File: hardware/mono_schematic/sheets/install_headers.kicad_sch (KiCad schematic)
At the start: 66 parts

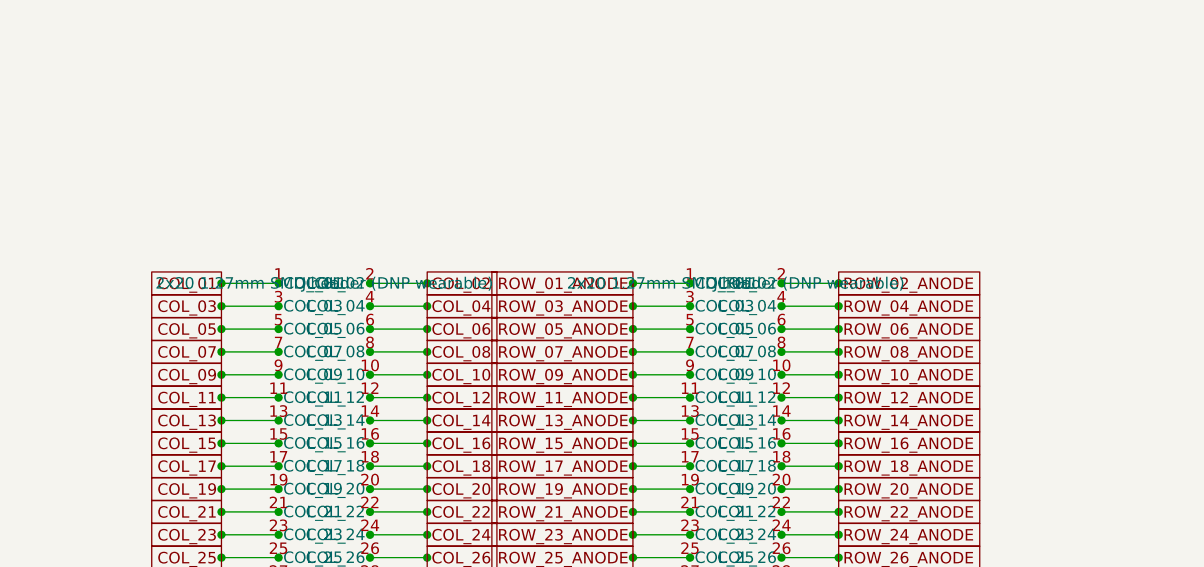
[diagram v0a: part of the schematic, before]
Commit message: mono_electronics v14b: installation headers -> XFCN BH127VS-40P-H49 2x20 1.27mm shrouded keyed box headers (C42462832; mate IDC3-40232A1EUB1 C49232620 + 0.635mm ribbon), 1:1 FFC pinout, 64 TVS kept; board 159.45x99.5 (was 160.5); gates clean; BOM/CPL variants + fab v14 regen
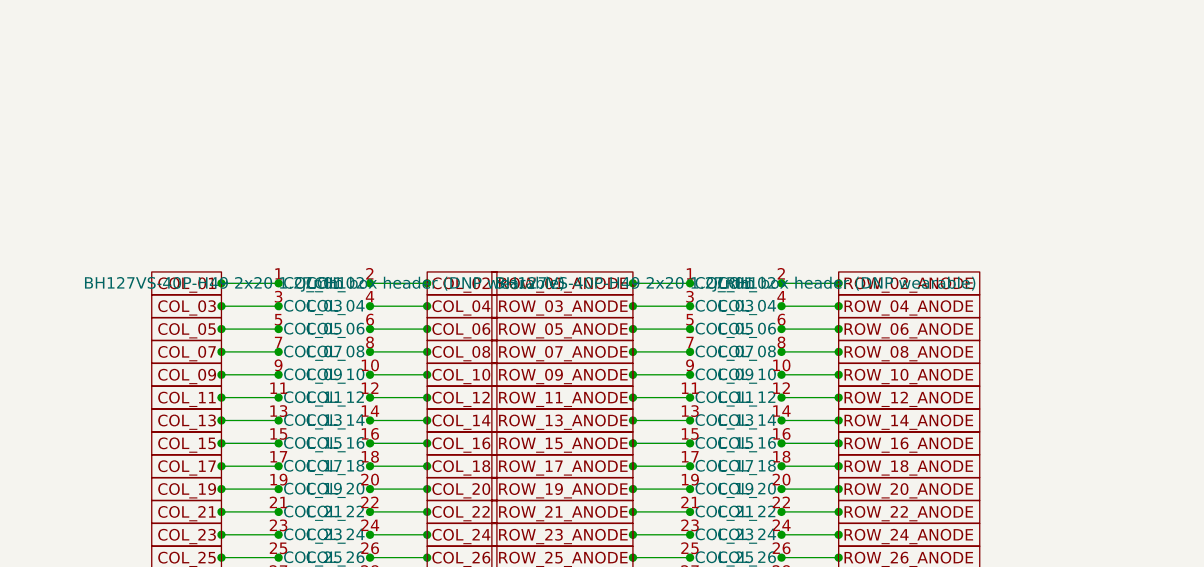
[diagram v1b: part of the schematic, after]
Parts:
- removed J_CH1, J_RH1: 2x20 1.27mm SMD header (DNP wearable), mono_electronics:PinHeader_2x20_P1.27mm_Vertical_SMD, symbol mono_parts:2x20_1.27mm_SMD_header__DNP_wearable__PinHeader_2x20_P1.27mm_Vertica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
- added J_CH1, J_RH1: BH127VS-40P-H49 2x20 1.27mm box header (DNP weara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, mono_electronics:BoxHeader_XFCN_BH127VS-40P-H49_2x20_P1.27mm_Vertical_SMD, symbol mono_parts:BH127VS-40P-H49_2x20_1.27mm_box_header__DNP_wearable__BoxHeader_XFCN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
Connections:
- net COL_01: now also J_CH1.1 (COL_01)
- net COL_02: now also J_CH1.2 (COL_02)
- net COL_03: now also J_CH1.3 (COL_03)
- net COL_04: now also J_CH1.4 (COL_04)
- net COL_05: now also J_CH1.5 (COL_05)
- net COL_06: now also J_CH1.6 (COL_06)
- net COL_07: now also J_CH1.7 (COL_07)
- net COL_08: now also J_CH1.8 (COL_08)
- net COL_09: now also J_CH1.9 (COL_09)
- net COL_10: now also J_CH1.10 (COL_10)
- net COL_11: now also J_CH1.11 (COL_11)
- net COL_12: now also J_CH1.12 (COL_12)
- net COL_13: now also J_CH1.13 (COL_13)
- net COL_14: now also J_CH1.14 (COL_14)
- net COL_15: now also J_CH1.15 (COL_15)
- net COL_16: now also J_CH1.16 (COL_16)
- net COL_17: now also J_CH1.17 (COL_17)
- net COL_18: now also J_CH1.18 (COL_18)
- net COL_19: now also J_CH1.19 (COL_19)
- net COL_20: now also J_CH1.20 (COL_20)
- net COL_21: now also J_CH1.21 (COL_21)
- net COL_22: now also J_CH1.22 (COL_22)
- net COL_23: now also J_CH1.23 (COL_23)
- net COL_24: now also J_CH1.24 (COL_24)
- net COL_25: now also J_CH1.25 (COL_25)
- net COL_26: now also J_CH1.26 (COL_26)
- net COL_27: now also J_CH1.27 (COL_27)
- net COL_28: now also J_CH1.28 (COL_28)
- net COL_29: now also J_CH1.29 (COL_29)
- net COL_30: now also J_CH1.30 (COL_30)
- net COL_31: now also J_CH1.31 (COL_31)
- net COL_32: now also J_CH1.32 (COL_32)
- net EXP_3V3: now also J_CH1.39 (EXP_3V3)
- net EXP_CLK: now also J_CH1.35 (EXP_CLK)
- net EXP_LE: now also J_CH1.36 (EXP_LE)
- net EXP_OE: now also J_CH1.37 (EXP_OE)
- net EXP_SDI: now also J_CH1.34 (EXP_SDI)
- net GND: now also J_CH1.33 (GND), J_CH1.38 (GND), J_CH1.40 (GND), J_RH1.33 (GND), J_RH1.38 (GND), J_RH1.40 (GND)
- net ID_3V3: now also J_RH1.37 (EXP_OE)
- net ID_SCL: now also J_RH1.36 (EXP_LE)
- net ID_SDA: now also J_RH1.35 (EXP_CLK)
- net ROW_01_ANODE: now also J_RH1.1 (COL_01)
- net ROW_02_ANODE: now also J_RH1.2 (COL_02)
- net ROW_03_ANODE: now also J_RH1.3 (COL_03)
- net ROW_04_ANODE: now also J_RH1.4 (COL_04)
- net ROW_05_ANODE: now also J_RH1.5 (COL_05)
- net ROW_06_ANODE: now also J_RH1.6 (COL_06)
- net ROW_07_ANODE: now also J_RH1.7 (COL_07)
- net ROW_08_ANODE: now also J_RH1.8 (COL_08)
- net ROW_09_ANODE: now also J_RH1.9 (COL_09)
- net ROW_10_ANODE: now also J_RH1.10 (COL_10)
- net ROW_11_ANODE: now also J_RH1.11 (COL_11)
- net ROW_12_ANODE: now also J_RH1.12 (COL_12)
- net ROW_13_ANODE: now also J_RH1.13 (COL_13)
- net ROW_14_ANODE: now also J_RH1.14 (COL_14)
- net ROW_15_ANODE: now also J_RH1.15 (COL_15)
- net ROW_16_ANODE: now also J_RH1.16 (COL_16)
- net ROW_17_ANODE: now also J_RH1.17 (COL_17)
- net ROW_18_ANODE: now also J_RH1.18 (COL_18)
- net ROW_19_ANODE: now also J_RH1.19 (COL_19)
- net ROW_20_ANODE: now also J_RH1.20 (COL_20)
- net ROW_21_ANODE: now also J_RH1.21 (COL_21)
- net ROW_22_ANODE: now also J_RH1.22 (COL_22)
- net ROW_23_ANODE: now also J_RH1.23 (COL_23)
- net ROW_24_ANODE: now also J_RH1.24 (COL_24)
- net ROW_25_ANODE: now also J_RH1.25 (COL_25)
- net ROW_26_ANODE: now also J_RH1.26 (COL_26)
- net ROW_27_ANODE: now also J_RH1.27 (COL_27)
- net ROW_28_ANODE: now also J_RH1.28 (COL_28)
- net ROW_29_ANODE: now also J_RH1.29 (COL_29)
- net ROW_30_ANODE: now also J_RH1.30 (COL_30)
- net ROW_31_ANODE: now also J_RH1.31 (COL_31)
- net ROW_32_ANODE: now also J_RH1.32 (COL_32)
- net ROW_SPARE_34: now also J_RH1.34 (EXP_SDI)
- net ROW_SPARE_39: now also J_RH1.39 (EXP_3V3)
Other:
- title: Installation-build cable headers (v14, DNP in wearable) - J_RH1/J_CH1 2x20 1.27 mm SMD in parallel with J_ROW1/J_COL1 pin-for-pin, PESD5V0S1BL per LED line -> Installation-build cable headers (v14, DNP in wearable) - J_RH1/J_CH1 2x20 1.27 mm shrouded keyed box headers (XFCN BH127VS-40P-H49) in parallel with J_ROW1/J_COL1 pin-for-pin, PESD5V0S1BL per LED line

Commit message: mono_electronics v15b: standalone project projects/mono_electronics_v15 (KiCad sch+pcb+libs+3D, fab, drawings, renders, docs); D_VBUS1 next to J_USB1, SYS 0.6 mm + doubled vias, 3 fiducials, silk 0.15, J_PORT courtyards inside edge, 1.6 mm JLC04161H-7628 stackup, 24 sub-0.127 mm gaps fixed (min_clearance 0.127), sch DNP/BOM attrs + lib nicknames -> native parity 0; DRC 0 ERC 0 continuity 312/312
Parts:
- D_C01, D_C02, D_C03, D_C04, D_C05, D_C06, D_C07, D_C08, D_C09, D_C10, D_C11, D_C12, D_C13, D_C14, D_C15, D_C16, D_C17, D_C18, D_C19, D_C20, D_C21, D_C22, D_C23, D_C24, D_C25, D_C26, D_C27, D_C28, D_C29, D_C30, D_C31, D_C32, D_R01, D_R02, D_R03, D_R04, D_R05, D_R06, D_R07, D_R08, D_R09, D_R10, D_R11, D_R12, D_R13, D_R14, D_R15, D_R16, D_R17, D_R18, D_R19, D_R20, D_R21, D_R22, D_R23, D_R24, D_R25, D_R26, D_R27, D_R28, D_R29, D_R30, D_R31, D_R32, J_CH1, J_RH1: now not fitted
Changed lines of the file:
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@@
     (on_board yes)
     (in_pos_files yes)
-    (dnp no)
+    (dnp yes)
     (property
       "Reference"
@@
     (on_board yes)
     (in_pos_files yes)
-    (dnp no)
+    (dnp yes)
     (property
       "Reference"
@@
     (on_board yes)
     (in_pos_files yes)
-    (dnp no)
+    (dnp yes)
     (property
       "Reference"
@@
     (on_board yes)
     (in_pos_files yes)
-    (dnp no)
+    (dnp yes)
     (property
       "Reference"
@@
     (on_board yes)
     (in_pos_files yes)
-    (dnp no)
+    (dnp yes)
     (property
       "Reference"
@@
     (on_board yes)
     (in_pos_files yes)
-    (dnp no)
+    (dnp yes)
     (property
       "Reference"
@@
     (on_board yes)
     (in_pos_files yes)
-    (dnp no)
+    (dnp yes)
     (property
       "Reference"
@@
     (on_board yes)
     (in_pos_files yes)
-    (dnp no)
+    (dnp yes)
     (property
       "Reference"
@@
     (on_board yes)
     (in_pos_files yes)
-    (dnp no)
+    (dnp yes)
     (property
       "Reference"
@@
     (on_board yes)
     (in_pos_files yes)
-    (dnp no)
+    (dnp yes)
     (property
       "Reference"
@@
     (on_board yes)
     (in_pos_files yes)
-    (dnp no)
+    (dnp yes)
     (property
       "Reference"
@@
     (on_board yes)
     (in_pos_files yes)
-    (dnp no)
+    (dnp yes)
     (property
       "Reference"
@@
     (on_board yes)
     (in_pos_files yes)
-    (dnp no)
+    (dnp yes)
     (property
       "Reference"
@@
     (on_board yes)
     (in_pos_files yes)
-    (dnp no)
+    (dnp yes)
     (property
       "Reference"
@@
     (on_board yes)
     (in_pos_files yes)
-    (dnp no)
+    (dnp yes)
     (property
       "Reference"
@@
     (on_board yes)
     (in_pos_files yes)
-    (dnp no)
+    (dnp yes)
     (property
       "Reference"
@@
     (on_board yes)
     (in_pos_files yes)
-    (dnp no)
+    (dnp yes)
     (property
       "Reference"
@@
     (on_board yes)
     (in_pos_files yes)
-    (dnp no)
+    (dnp yes)
     (property
       "Reference"
@@
     (on_board yes)
     (in_pos_files yes)
-    (dnp no)
+    (dnp yes)
     (property
       "Reference"
@@
     (on_board yes)
     (in_pos_files yes)
-    (dnp no)
+    (dnp yes)
     (property
       "Reference"
@@
     (on_board yes)
     (in_pos_files yes)
-    (dnp no)
+    (dnp yes)
     (property
       "Reference"
@@
     (on_board yes)
     (in_pos_files yes)
-    (dnp no)
+    (dnp yes)
     (property
       "Reference"
@@
     (on_board yes)
     (in_pos_files yes)
-    (dnp no)
+    (dnp yes)
     (property
       "Reference"
@@
     (on_board yes)
     (in_pos_files yes)
-    (dnp no)
+    (dnp yes)
     (property
       "Reference"
@@
     (on_board yes)
     (in_pos_files yes)
-    (dnp no)
+    (dnp yes)
     (property
       "Reference"
@@
     (on_board yes)
     (in_pos_files yes)
-    (dnp no)
+    (dnp yes)
     (property
       "Reference"
@@
     (on_board yes)
     (in_pos_files yes)
-    (dnp no)
+    (dnp yes)
     (property
       "Reference"
@@
     (on_board yes)
     (in_pos_files yes)
-    (dnp no)
+    (dnp yes)
     (property
       "Reference"
@@
     (on_board yes)
     (in_pos_files yes)
-    (dnp no)
+    (dnp yes)
     (property
       "Reference"
@@
     (on_board yes)
     (in_pos_files yes)
-    (dnp no)
+    (dnp yes)
     (property
       "Reference"
@@
     (on_board yes)
     (in_pos_files yes)
-    (dnp no)
+    (dnp yes)
     (property
       "Reference"
@@
     (on_board yes)
     (in_pos_files yes)
-    (dnp no)
+    (dnp yes)
     (property
       "Reference"
@@
     (on_board yes)
     (in_pos_files yes)
-    (dnp no)
+    (dnp yes)
     (property
       "Reference"
@@
     (on_board yes)
     (in_pos_files yes)
-    (dnp no)
+    (dnp yes)
     (property
       "Reference"
@@
     (on_board yes)
     (in_pos_files yes)
-    (dnp no)
+    (dnp yes)
     (property
       "Reference"
@@
     (on_board yes)
     (in_pos_files yes)
-    (dnp no)
+    (dnp yes)
     (property
       "Reference"
@@
     (on_board yes)
     (in_pos_files yes)
-    (dnp no)
+    (dnp yes)
     (property
       "Reference"
@@
     (on_board yes)
     (in_pos_files yes)
-    (dnp no)
+    (dnp yes)
     (property
       "Reference"
@@
     (on_board yes)
     (in_pos_files yes)
-    (dnp no)
+    (dnp yes)
     (property
       "Reference"
@@
     (on_board yes)
     (in_pos_files yes)
-    (dnp no)
+    (dnp yes)
     (property
       "Reference"
@@
     (on_board yes)
     (in_pos_files yes)
-    (dnp no)
+    (dnp yes)
     (property
       "Reference"
@@
     (on_board yes)
     (in_pos_files yes)
-    (dnp no)
+    (dnp yes)
     (property
       "Reference"
@@
     (on_board yes)
     (in_pos_files yes)
-    (dnp no)
+    (dnp yes)
     (property
       "Reference"
@@
     (on_board yes)
     (in_pos_files yes)
-    (dnp no)
+    (dnp yes)
     (property
       "Reference"
@@
     (on_board yes)
     (in_pos_files yes)
-    (dnp no)
+    (dnp yes)
     (property
       "Reference"
@@
     (on_board yes)
     (in_pos_files yes)
-    (dnp no)
+    (dnp yes)
     (property
       "Reference"
@@
     (on_board yes)
     (in_pos_files yes)
-    (dnp no)
+    (dnp yes)
     (property
       "Reference"
@@
     (on_board yes)
     (in_pos_files yes)
-    (dnp no)
+    (dnp yes)
     (property
       "Reference"
@@
     (on_board yes)
     (in_pos_files yes)
-    (dnp no)
+    (dnp yes)
     (property
       "Reference"
@@
     (on_board yes)
     (in_pos_files yes)
-    (dnp no)
+    (dnp yes)
     (property
       "Reference"
@@
     (on_board yes)
     (in_pos_files yes)
-    (dnp no)
+    (dnp yes)
     (property
       "Reference"
@@
     (on_board yes)
     (in_pos_files yes)
-    (dnp no)
+    (dnp yes)
     (property
       "Reference"
@@
     (on_board yes)
     (in_pos_files yes)
-    (dnp no)
+    (dnp yes)
     (property
       "Reference"
@@
     (on_board yes)
     (in_pos_files yes)
-    (dnp no)
+    (dnp yes)
     (property
       "Reference"
@@
     (on_board yes)
     (in_pos_files yes)
-    (dnp no)
+    (dnp yes)
     (property
       "Reference"
@@
     (on_board yes)
     (in_pos_files yes)
-    (dnp no)
+    (dnp yes)
     (property
       "Reference"
@@
     (on_board yes)
     (in_pos_files yes)
-    (dnp no)
+    (dnp yes)
     (property
       "Reference"
@@
     (on_board yes)
     (in_pos_files yes)
-    (dnp no)
+    (dnp yes)
     (property
       "Reference"
@@
     (on_board yes)
     (in_pos_files yes)
-    (dnp no)
+    (dnp yes)
     (property
       "Reference"
@@
     (on_board yes)
     (in_pos_files yes)
-    (dnp no)
+    (dnp yes)
     (property
       "Reference"
@@
     (on_board yes)
     (in_pos_files yes)
-    (dnp no)
+    (dnp yes)
     (property
       "Reference"
@@
     (on_board yes)
     (in_pos_files yes)
-    (dnp no)
+    (dnp yes)
     (property
       "Reference"
@@
     (on_board yes)
     (in_pos_files yes)
-    (dnp no)
+    (dnp yes)
     (property
       "Reference"
@@
     (on_board yes)
     (in_pos_files yes)
-    (dnp no)
+    (dnp yes)
     (property
       "Reference"
@@
     (on_board yes)
     (in_pos_files yes)
-    (dnp no)
+    (dnp yes)
     (property
       "Reference"
@@
     (on_board yes)
     (in_pos_files yes)
-    (dnp no)
+    (dnp yes)
     (property
       "Reference"
